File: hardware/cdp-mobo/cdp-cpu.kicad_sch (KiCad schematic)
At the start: 21 parts, among them U1 CDP1802ACE, U2 74HC132, U3 74HC573, U4 W24512AK-20, U5 2764

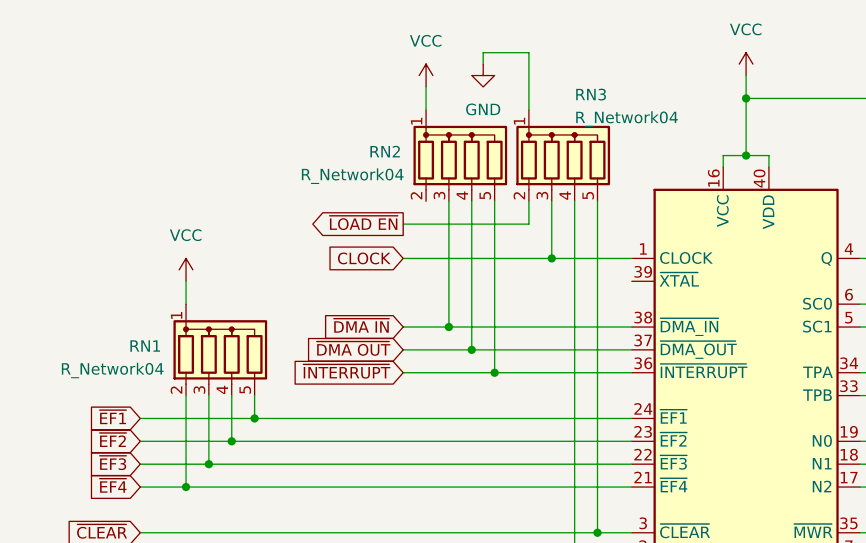
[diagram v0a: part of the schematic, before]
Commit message: Minor changes in component values, and added a the IO module.
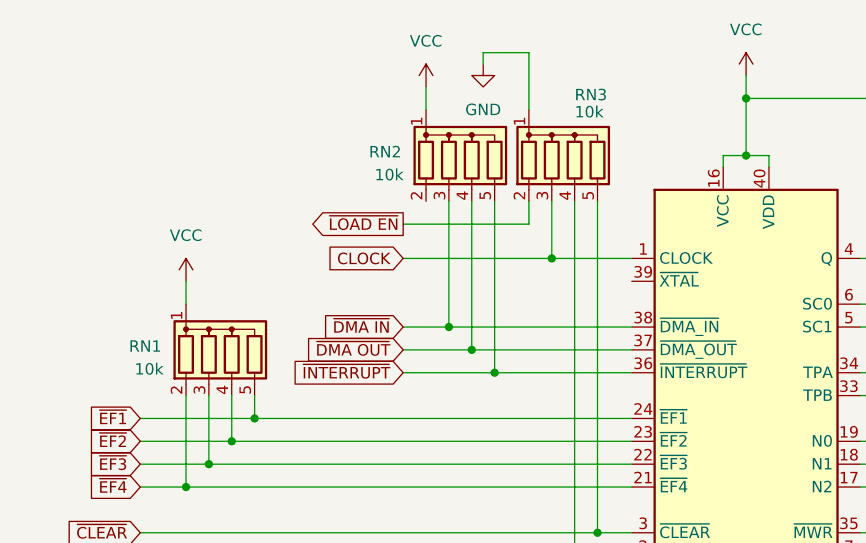
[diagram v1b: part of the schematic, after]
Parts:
- RN1, RN2, RN3: value R_Network04 -> 10k
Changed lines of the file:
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@@
       (effects (font (size 1.27 1.27)) (justify left))
     )
-    (property "Value" "R_Network04" (at 15.24 51.689 0)
+    (property "Value" "10k" (at 23.495 51.689 0)
       (effects (font (size 1.27 1.27)) (justify left))
     )
@@
       (effects (font (size 1.27 1.27)) (justify left))
     )
-    (property "Value" "R_Network04" (at 72.39 23.749 0)
+    (property "Value" "10k" (at 72.39 23.114 0)
       (effects (font (size 1.27 1.27)) (justify left))
     )
@@
       (effects (font (size 1.27 1.27)) (justify left))
     )
-    (property "Value" "R_Network04" (at 41.91 30.099 0)
-      (effects (font (size 1.27 1.27)) (justify left))
-    )
+    (property "Value" "10k" (at 50.165 30.099 0)
+      (effects (font (size 1.27 1.27)) (justify left))
+    )
